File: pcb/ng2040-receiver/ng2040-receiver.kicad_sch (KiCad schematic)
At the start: 16 parts, among them J1 DB15_F, SW1 OPTS, U1 RP2040-Zero, U2 NRF24L01_Breakout

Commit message: WIP moving radio to top of receiver
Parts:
- added C3: 0.1uF, Capacitor_SMD:C_0805_2012Metric_Pad1.18x1.45mm_HandSolder, symbol Device:C
- added C4: 10uF, Capacitor_SMD:C_0805_2012Metric_Pad1.18x1.45mm_HandSolder, symbol Device:C
- C2: value 0.1uF -> 10nF
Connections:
- net 3V3: now also C3.2, C4.1
- net GND: now also C3.1, C4.2
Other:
- moved on the sheet: C1, C2

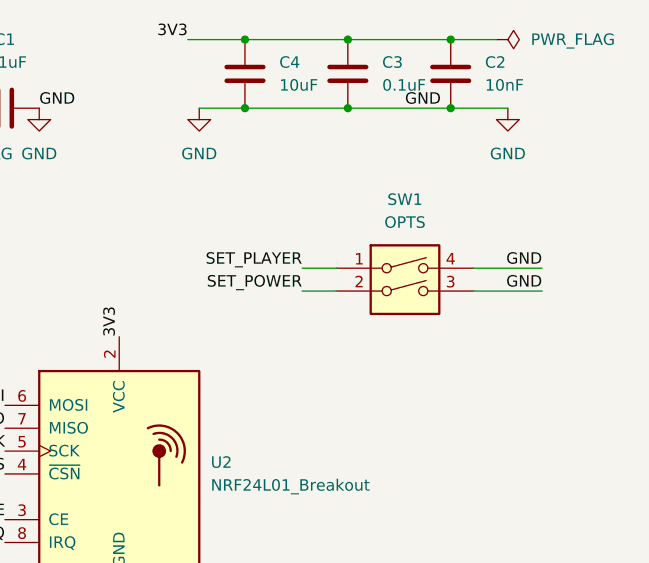
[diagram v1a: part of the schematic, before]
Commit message: trimming receiver board
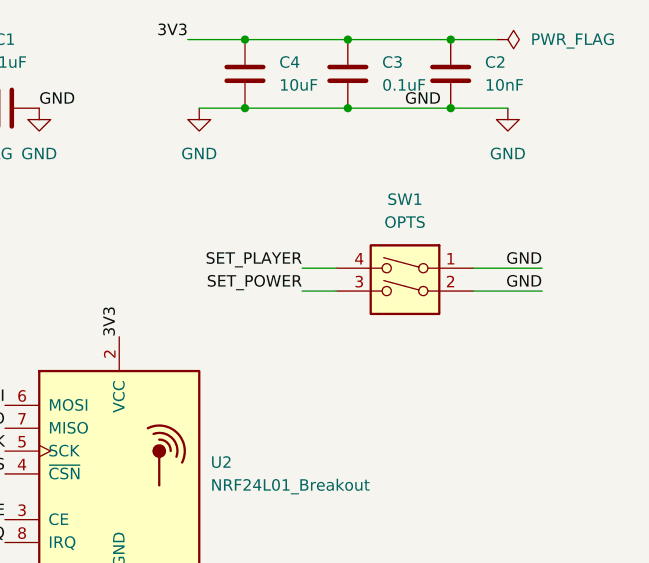
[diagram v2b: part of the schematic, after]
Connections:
- net GND: now also SW1.1, SW1.2; no longer SW1.3, SW1.4
- net SET_PLAYER: now also SW1.4; no longer SW1.1
- net SET_POWER: now also SW1.3; no longer SW1.2
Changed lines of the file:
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@@
 		(lib_id "Switch:SW_DIP_x02")
 		(at 198.12 48.26 0)
+		(mirror y)
 		(unit 1)
 		(exclude_from_sim no)
@@
 		(on_board yes)
 		(dnp no)
-		(fields_autoplaced yes)
 		(property "Reference" "SW1"
 			(at 198.12 38.1 0)

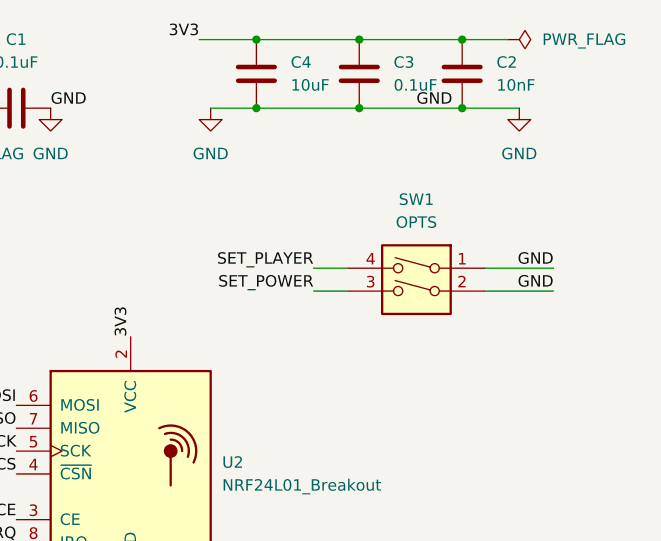
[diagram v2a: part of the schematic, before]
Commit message: Rerouting
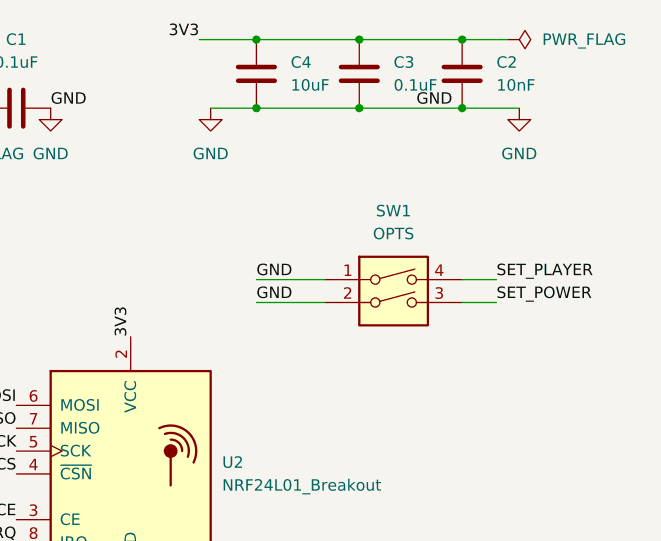
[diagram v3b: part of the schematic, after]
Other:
- moved on the sheet: SW1
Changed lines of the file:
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@@
 	(wire
 		(pts
-			(xy 205.74 45.72) (xy 213.36 45.72)
+			(xy 187.96 46.99) (xy 180.34 46.99)
 		)
 		(stroke
@@
 	(wire
 		(pts
-			(xy 186.69 48.26) (xy 190.5 48.26)
+			(xy 207.01 49.53) (xy 203.2 49.53)
 		)
 		(stroke
@@
 	(wire
 		(pts
-			(xy 186.69 45.72) (xy 190.5 45.72)
+			(xy 207.01 46.99) (xy 203.2 46.99)
 		)
 		(stroke
@@
 	(wire
 		(pts
-			(xy 205.74 48.26) (xy 213.36 48.26)
+			(xy 187.96 49.53) (xy 180.34 49.53)
 		)
 		(stroke
@@
 	)
 	(label "GND"
-		(at 213.36 45.72 180)
-		(fields_autoplaced yes)
-		(effects
-			(font
-				(size 1.27 1.27)
-			)
-			(justify right bottom)
+		(at 180.34 46.99 0)
+		(fields_autoplaced yes)
+		(effects
+			(font
+				(size 1.27 1.27)
+			)
+			(justify left bottom)
 		)
 	)
@@
 	)
 	(label "GND"
-		(at 213.36 48.26 180)
-		(fields_autoplaced yes)
-		(effects
-			(font
-				(size 1.27 1.27)
-			)
-			(justify right bottom)
+		(at 180.34 49.53 0)
+		(fields_autoplaced yes)
+		(effects
+			(font
+				(size 1.27 1.27)
+			)
+			(justify left bottom)
 		)
 	)
@@
 	)
 	(label "SET_PLAYER"
-		(at 186.69 45.72 180)
-		(fields_autoplaced yes)
-		(effects
-			(font
-				(size 1.27 1.27)
-			)
-			(justify right bottom)
+		(at 207.01 46.99 0)
+		(fields_autoplaced yes)
+		(effects
+			(font
+				(size 1.27 1.27)
+			)
+			(justify left bottom)
 		)
 	)
@@
 	)
 	(label "SET_POWER"
-		(at 186.69 48.26 180)
-		(fields_autoplaced yes)
-		(effects
-			(font
-				(size 1.27 1.27)
-			)
-			(justify right bottom)
+		(at 207.01 49.53 0)
+		(fields_autoplaced yes)
+		(effects
+			(font
+				(size 1.27 1.27)
+			)
+			(justify left bottom)
 		)
 	)
@@
 	(symbol
 		(lib_id "Switch:SW_DIP_x02")
-		(at 198.12 48.26 0)
-		(mirror y)
+		(at 195.58 49.53 0)
 		(unit 1)
 		(exclude_from_sim no)
@@
 		(dnp no)
 		(property "Reference" "SW1"
-			(at 198.12 38.1 0)
+			(at 195.58 39.37 0)
 			(effects
 				(font
@@
 		)
 		(property "Value" "OPTS"
-			(at 198.12 40.64 0)
+			(at 195.58 41.91 0)
 			(effects
 				(font
@@
 		)
 		(property "Footprint" "Button_Switch_SMD:SW_DIP_SPSTx02_Slide_6.7x6.64mm_W8.61mm_P2.54mm_LowProfile"
-			(at 198.12 48.26 0)
+			(at 195.58 49.53 0)
 			(effects
 				(font
@@
 		)
 		(property "Datasheet" "~"
-			(at 198.12 48.26 0)
+			(at 195.58 49.53 0)
 			(effects
 				(font
@@
 		)
 		(property "Description" "2x DIP Switch, Single Pole Single Throw (SPST) switch, small symbol"
-			(at 198.12 48.26 0)
+			(at 195.58 49.53 0)
 			(effects
 				(font
@@
 		)
 		(property "Notes" ""
-			(at 198.12 48.26 0)
-			(effects
-				(font
+			(at 195.58 49.53 0)
+			(effects
+				(font
